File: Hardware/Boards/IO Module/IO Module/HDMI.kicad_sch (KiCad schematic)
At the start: 62 parts, among them J4 HDMI_A, U10 TPD4E02B04DQA, U19 TPS74801AWDRC, U20 PCA9517ATP, U21 TXB0108DQSR, U25 TPD4E02B04DQA, U27 L78L05_SOT89, U5 SN75DP159RSB, U7 TPD5S116

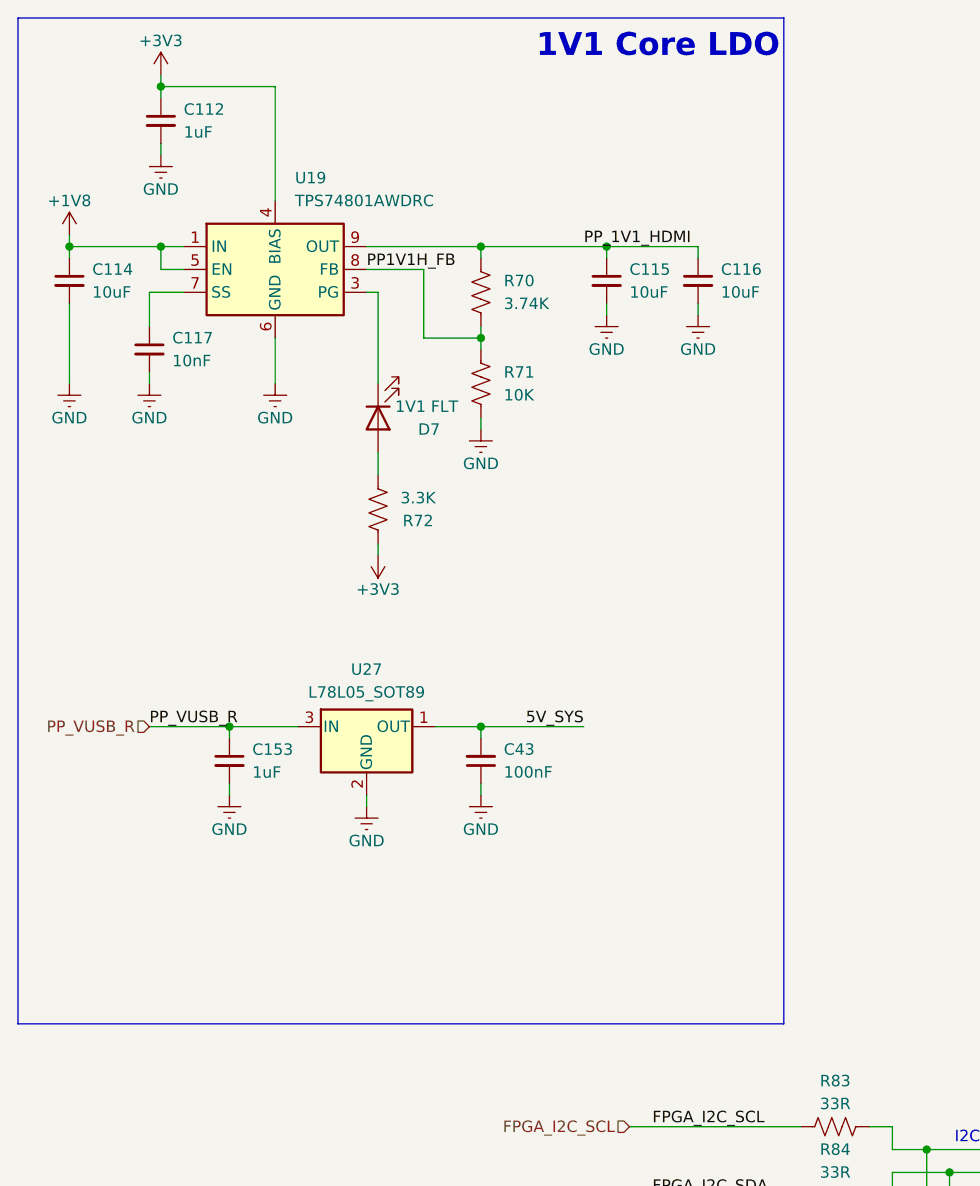
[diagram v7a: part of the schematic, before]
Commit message: Cleaned up IO Module and went through DRC errors
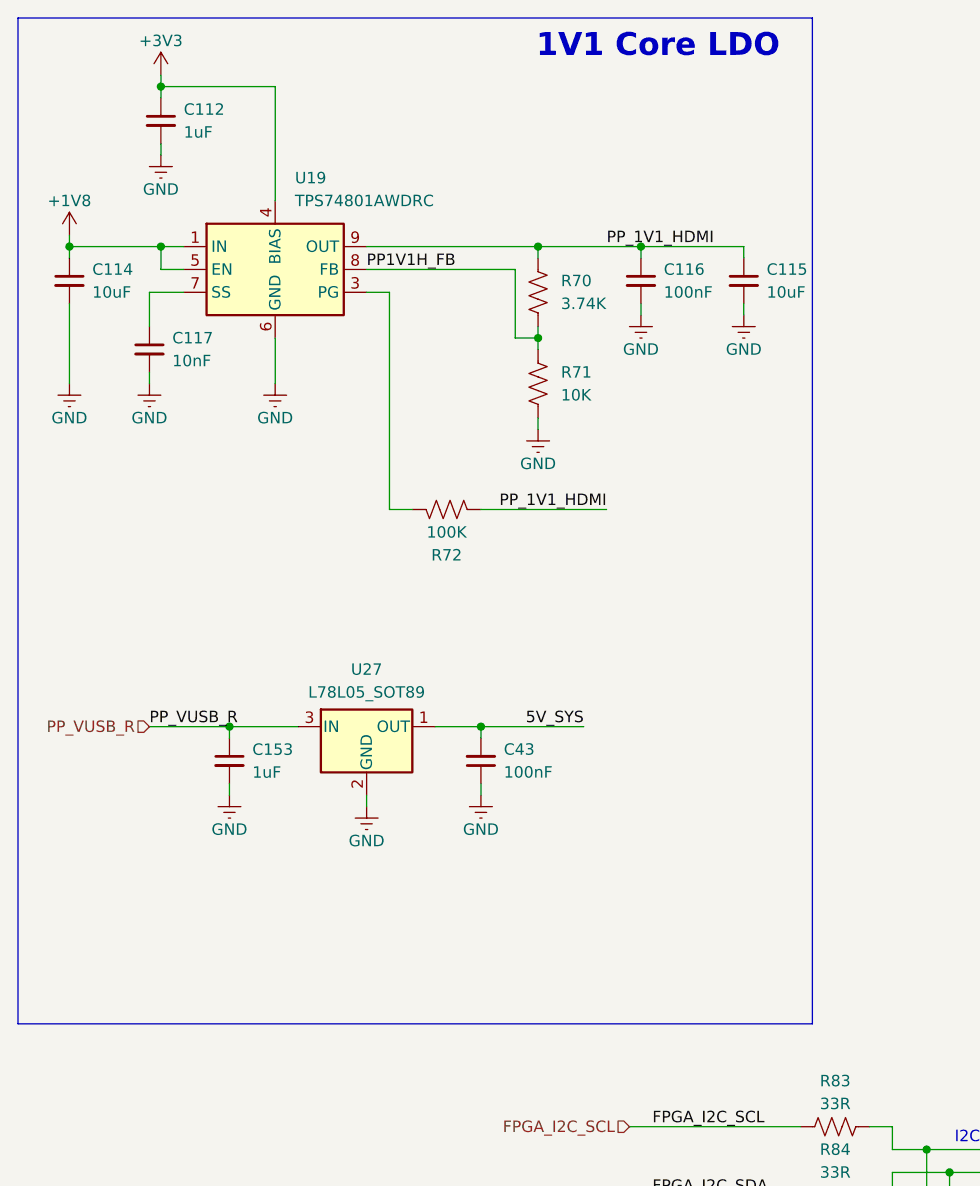
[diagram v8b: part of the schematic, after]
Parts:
- removed D7: 1V1 FLT, LED_SMD:LED_0603_1608Metric, symbol Device:LED
- C116: value 10uF -> 100nF; footprint Capacitor_SMD:C_0603_1608Metric -> Capacitor_SMD:C_0201_0603Metric
- R72: value 3.3K -> 100K
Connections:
- net +3V3: no longer R72.1
- net PP_1V1_HDMI: now also R72.1
- net at R72.2: now also U19.3 (PG)
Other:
- moved on the sheet: C115, C116, R70, R71
